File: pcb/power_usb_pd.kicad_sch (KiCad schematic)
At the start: 0 parts

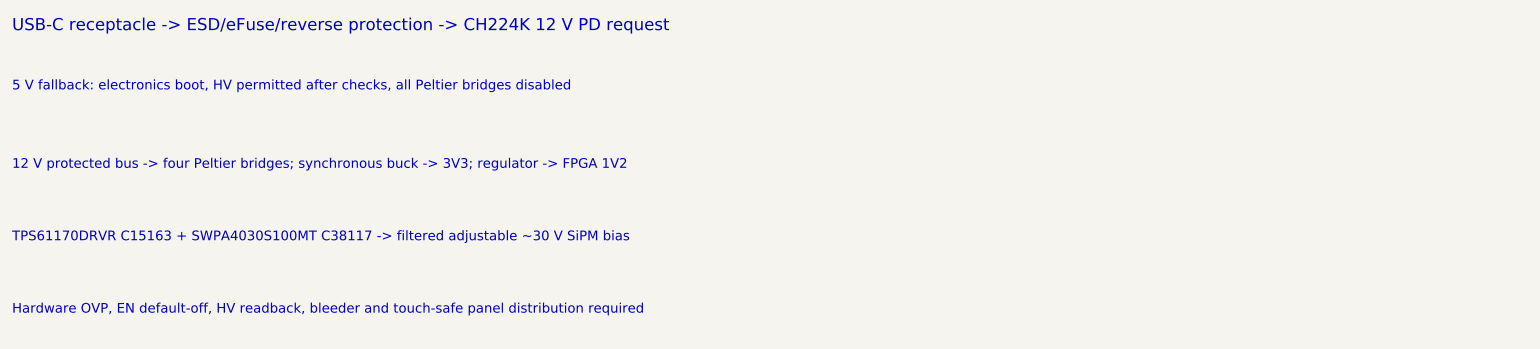
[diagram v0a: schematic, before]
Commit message: Update everything: layman summaries, Google Photos/Drive connectors for docs/sims/data/tests, multi-account support, rclone integration, enhanced pull scripts, PCB design refinements, Muon3Vision assets, 3D models, build improvements
- Added/updated layman summaries in main READMEs (physics, pcb, Muon3Vision, sim)
- Full Google Photos connector with date/keyword filtering to explore library for data and tests
- New Google Drive pull script for simulations and additional information
- Support for all accounts via separate OAuth / rclone remotes
- Installed rclone; documented connectors after system check (no desktop sync active)
- Updated scripts/, .gitignore, build_paper.sh --pull-images, main docs
- PCB architecture updates (power, DACs, hardware TEC safety, telemetry RP2040)
- Added missing part READMEs and 3D models
- Muon3Vision resources and Package.swift

All changes documented and ready for use.
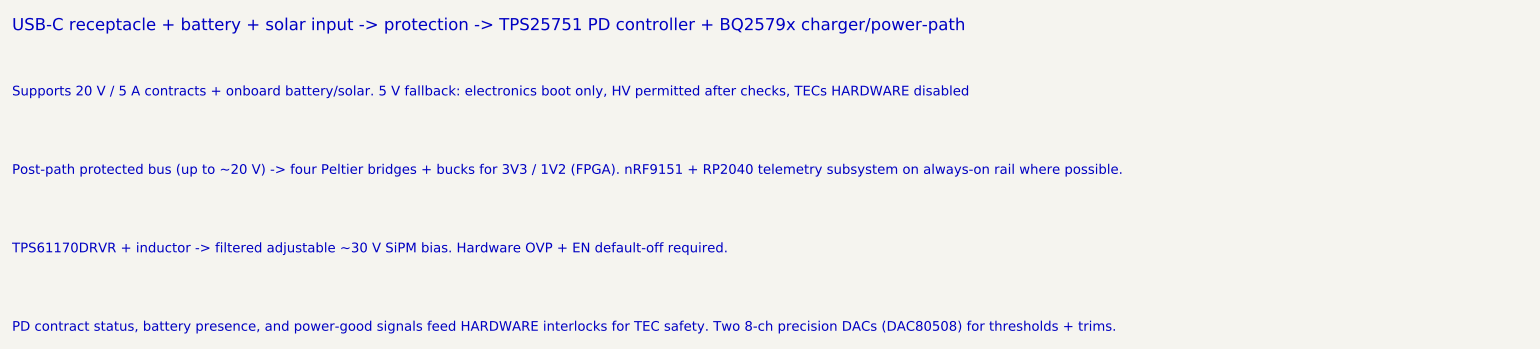
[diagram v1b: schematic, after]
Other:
- note added: "PD contract status, battery presence, and power-good signals feed HARDWARE interlocks for TEC safety. Two 8-ch precision DACs (DAC80508) for thresholds + trims."
- note added: "Post-path protected bus (up to ~20 V) -> four Peltier bridges + bucks for 3V3 / 1V2 (FPGA). nRF9151 + RP2040 telemetry subsystem on always-on rail where possible."
- note added: "Supports 20 V / 5 A contracts + onboard battery/solar. 5 V fallback: electronics boot only, HV permitted after checks, TECs HARDWARE disabled"
- note added: "TPS61170DRVR + inductor -> filtered adjustable ~30 V SiPM bias. Hardware OVP + EN default-off required."
- note added: "USB-C receptacle + battery + solar input -> protection -> TPS25751 PD controller + BQ2579x charger/power-path"
- note removed: "12 V protected bus -> four Peltier bridges; synchronous buck -> 3V3; regulator -> FPGA 1V2"
- note removed: "5 V fallback: electronics boot, HV permitted after checks, all Peltier bridges disabled"
- note removed: "Hardware OVP, EN default-off, HV readback, bleeder and touch-safe panel distribution required"
- note removed: "TPS61170DRVR C15163 + SWPA4030S100MT C38117 -> filtered adjustable ~30 V SiPM bias"
- note removed: "USB-C receptacle -> ESD/eFuse/reverse protection -> CH224K 12 V PD request"
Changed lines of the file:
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@@
  (paper "A3")
   (title_block (title "Muon3 power, USB-C PD and SiPM bias") (date "2026-07-11") (rev "P0") (comment 1 "ARCHITECTURE - electrical capture pending"))
-  (text "USB-C receptacle -> ESD/eFuse/reverse protection -> CH224K 12 V PD request" (at 25 35 0) (effects (font (size 2 2)) (justify left)))
-  (text "5 V fallback: electronics boot, HV permitted after checks, all Peltier bridges disabled" (at 25 45 0) (effects (font (size 1.6 1.6)) (justify left)))
-  (text "12 V protected bus -> four Peltier bridges; synchronous buck -> 3V3; regulator -> FPGA 1V2" (at 25 58 0) (effects (font (size 1.6 1.6)) (justify left)))
-  (text "TPS61170DRVR C15163 + SWPA4030S100MT C38117 -> filtered adjustable ~30 V SiPM bias" (at 25 70 0) (effects (font (size 1.6 1.6)) (justify left)))
-  (text "Hardware OVP, EN default-off, HV readback, bleeder and touch-safe panel distribution required" (at 25 82 0) (effects (font (size 1.6 1.6)) (justify left)))
+  (text "USB-C receptacle + battery + solar input -> protection -> TPS25751 PD controller + BQ2579x charger/power-path" (at 25 35 0) (effects (font (size 2 2)) (justify left)))
+  (text "Supports 20 V / 5 A contracts + onboard battery/solar. 5 V fallback: electronics boot only, HV permitted after checks, TECs HARDWARE disabled" (at 25 46 0) (effects (font (size 1.6 1.6)) (justify left)))
+  (text "Post-path protected bus (up to ~20 V) -> four Peltier bridges + bucks for 3V3 / 1V2 (FPGA). nRF9151 + RP2040 telemetry subsystem on always-on rail where possible." (at 25 59 0) (effects (font (size 1.6 1.6)) (justify left)))
+  (text "TPS61170DRVR + inductor -> filtered adjustable ~30 V SiPM bias. Hardware OVP + EN default-off required." (at 25 72 0) (effects (font (size 1.6 1.6)) (justify left)))
+  (text "PD contract status, battery presence, and power-good signals feed HARDWARE interlocks for TEC safety. Two 8-ch precision DACs (DAC80508) for thresholds + trims." (at 25 85 0) (effects (font (size 1.6 1.6)) (justify left)))
   (sheet_instances (path "/" (page "2"))) (embedded_fonts no)
 )

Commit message: Update paper with latest architecture, add openEMS EM simulations (RF, SI, PDN), update schematics with real symbols/wires, add 3D models and openEMS figures
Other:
- note removed: "PD contract status, battery presence, and power-good signals feed HARDWARE interlocks for TEC safety. Two 8-ch precision DACs (DAC80508) for thresholds + trims."
- note removed: "Post-path protected bus (up to ~20 V) -> four Peltier bridges + bucks for 3V3 / 1V2 (FPGA). nRF9151 + RP2040 telemetry subsystem on always-on rail where possible."
- note removed: "Supports 20 V / 5 A contracts + onboard battery/solar. 5 V fallback: electronics boot only, HV permitted after checks, TECs HARDWARE disabled"
- note removed: "TPS61170DRVR + inductor -> filtered adjustable ~30 V SiPM bias. Hardware OVP + EN default-off required."
- note removed: "USB-C receptacle + battery + solar input -> protection -> TPS25751 PD controller + BQ2579x charger/power-path"
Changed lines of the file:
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@@
-(kicad_sch (version 20250114) (generator "eeschema") (generator_version "9.0")
- (paper "A3")
-  (title_block (title "Muon3 power, USB-C PD and SiPM bias") (date "2026-07-11") (rev "P0") (comment 1 "ARCHITECTURE - electrical capture pending"))
-  (text "USB-C receptacle + battery + solar input -> protection -> TPS25751 PD controller + BQ2579x charger/power-path" (at 25 35 0) (effects (font (size 2 2)) (justify left)))
-  (text "Supports 20 V / 5 A contracts + onboard battery/solar. 5 V fallback: electronics boot only, HV permitted after checks, TECs HARDWARE disabled" (at 25 46 0) (effects (font (size 1.6 1.6)) (justify left)))
-  (text "Post-path protected bus (up to ~20 V) -> four Peltier bridges + bucks for 3V3 / 1V2 (FPGA). nRF9151 + RP2040 telemetry subsystem on always-on rail where possible." (at 25 59 0) (effects (font (size 1.6 1.6)) (justify left)))
-  (text "TPS61170DRVR + inductor -> filtered adjustable ~30 V SiPM bias. Hardware OVP + EN default-off required." (at 25 72 0) (effects (font (size 1.6 1.6)) (justify left)))
-  (text "PD contract status, battery presence, and power-good signals feed HARDWARE interlocks for TEC safety. Two 8-ch precision DACs (DAC80508) for thresholds + trims." (at 25 85 0) (effects (font (size 1.6 1.6)) (justify left)))
-  (sheet_instances (path "/" (page "2"))) (embedded_fonts no)
+(kicad_sch
+	(version 20260306)
+	(generator "eeschema")
+	(generator_version "10.0")
+	(paper "A3")
+	(title_block
+		(title "Muon3 power, USB-C PD and SiPM bias")
+		(date "2026-07-11")
+		(rev "P1")
+		(comment 1 "BASIC SCHEMATIC - WIP")
+	)
 )
